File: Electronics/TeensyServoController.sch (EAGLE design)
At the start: 96 parts, among them U1 TEENSY_3.1_ALLPINS, U12 MIC5225, U13 MIC5225, U2 AP3211KTR-G1, U3 AP3211KTR-G1, U4 AP3211KTR-G1, U5 AP2210N-3.3TRG1

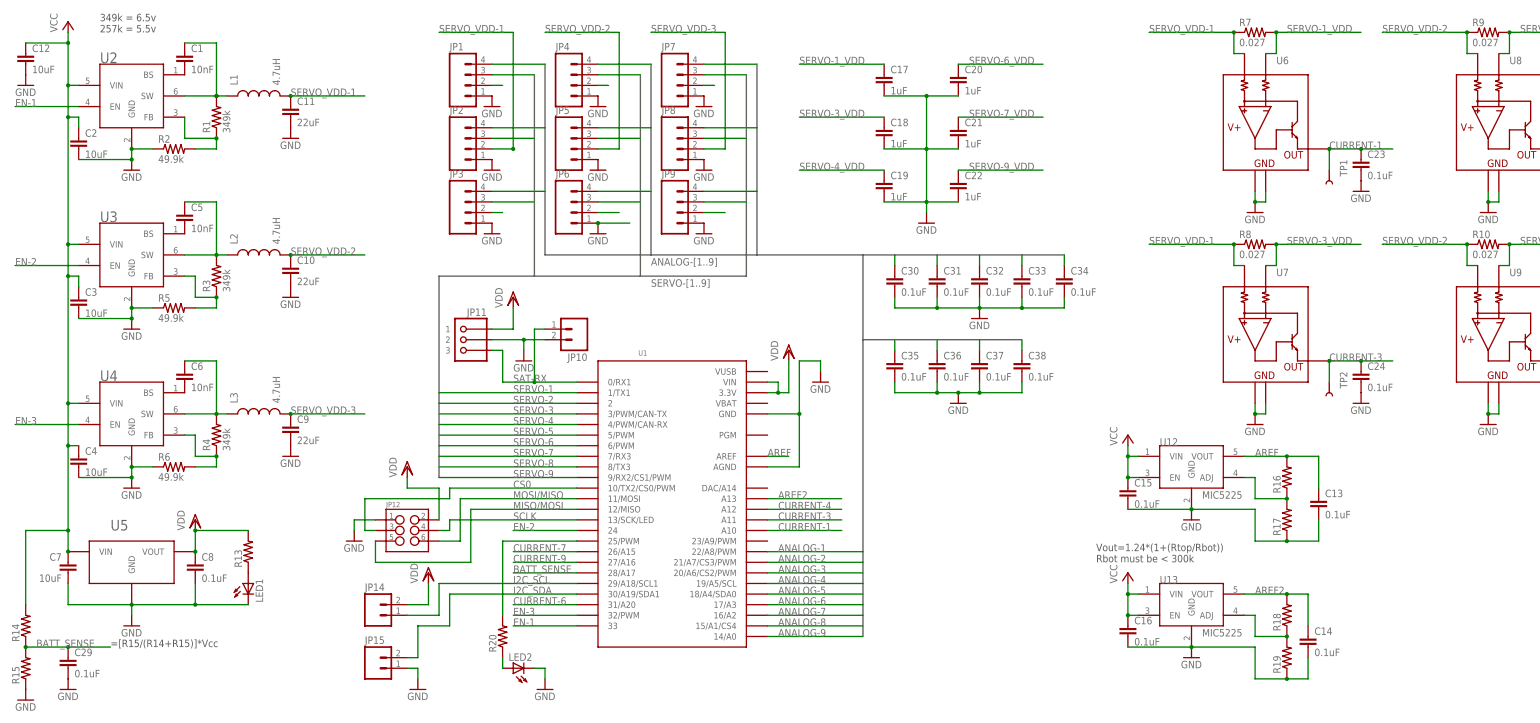
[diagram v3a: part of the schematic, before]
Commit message: Finalized values for most components on PCBs
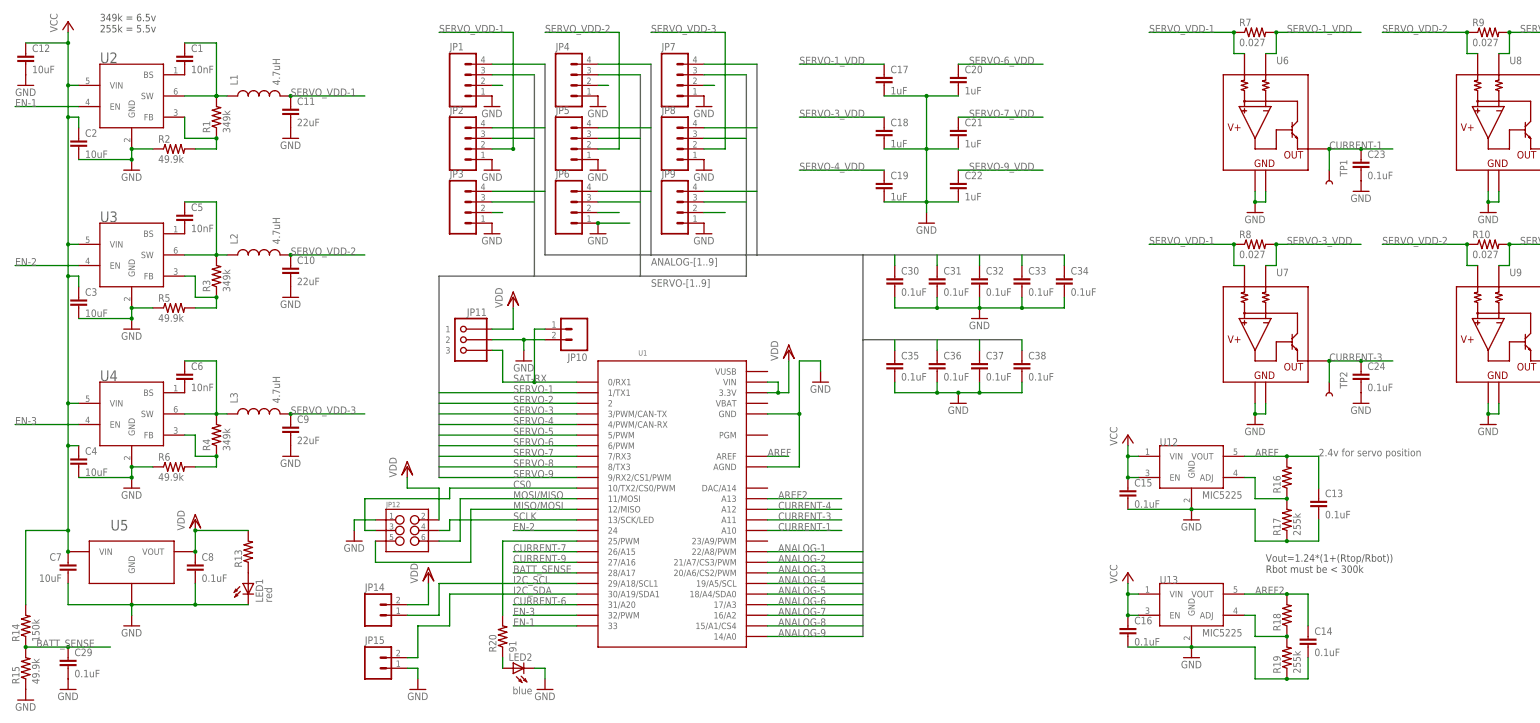
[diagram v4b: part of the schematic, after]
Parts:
- LED1: value (none) -> red
- LED2: value (none) -> blue
- R14: value (none) -> 150k
- R15: value (none) -> 49.9k
- R17, R19: value (none) -> 255k
- R20: value (none) -> 91
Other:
- note added: "2.4v for servo position"
- note added: "349k = 6.5v 255k = 5.5v"
- note removed: "349k = 6.5v 257k = 5.5v"
- note removed: "=[R15/(R14+R15)]*Vcc"
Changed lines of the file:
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@@
 <grid distance="0.1" unitdist="inch" unit="inch" style="lines" multiple="1" display="no" altdistance="0.01" altunitdist="inch" altunit="inch"/>
 <layers>
-<layer number="1" name="Top" color="4" fill="1" visible="yes" active="no"/>
-<layer number="2" name="Route2" color="5" fill="1" visible="yes" active="no"/>
-<layer number="3" name="Route3" color="4" fill="1" visible="yes" active="no"/>
-<layer number="14" name="Route14" color="1" fill="6" visible="yes" active="no"/>
-<layer number="15" name="Route15" color="3" fill="1" visible="yes" active="no"/>
-<layer number="16" name="Bottom" color="1" fill="1" visible="yes" active="no"/>
-<layer number="17" name="Pads" color="2" fill="1" visible="yes" active="no"/>
-<layer number="18" name="Vias" color="2" fill="1" visible="yes" active="no"/>
-<layer number="19" name="Unrouted" color="6" fill="1" visible="yes" active="no"/>
-<layer number="20" name="Dimension" color="15" fill="1" visible="yes" active="no"/>
-<layer number="21" name="tPlace" color="7" fill="1" visible="yes" active="no"/>
-<layer number="22" name="bPlace" color="7" fill="1" visible="yes" active="no"/>
-<layer number="23" name="tOrigins" color="15" fill="1" visible="yes" active="no"/>
-<layer number="24" name="bOrigins" color="15" fill="1" visible="yes" active="no"/>
-<layer number="25" name="tNames" color="7" fill="1" visible="yes" active="no"/>
-<layer number="26" name="bNames" color="7" fill="1" visible="yes" active="no"/>
-<layer number="27" name="tValues" color="7" fill="1" visible="yes" active="no"/>
-<layer number="28" name="bValues" color="7" fill="1" visible="yes" active="no"/>
+<layer number="1" name="Top" color="4" fill="1" visible="no" active="no"/>
+<layer number="2" name="Route2" color="5" fill="1" visible="no" active="no"/>
+<layer number="3" name="Route3" color="4" fill="1" visible="no" active="no"/>
+<layer number="14" name="Route14" color="1" fill="6" visible="no" active="no"/>
+<layer number="15" name="Route15" color="3" fill="1" visible="no" active="no"/>
+<layer number="16" name="Bottom" color="1" fill="1" visible="no" active="no"/>
+<layer number="17" name="Pads" color="2" fill="1" visible="no" active="no"/>
+<layer number="18" name="Vias" color="2" fill="1" visible="no" active="no"/>
+<layer number="19" name="Unrouted" color="6" fill="1" visible="no" active="no"/>
+<layer number="20" name="Dimension" color="15" fill="1" visible="no" active="no"/>
+<layer number="21" name="tPlace" color="7" fill="1" visible="no" active="no"/>
+<layer number="22" name="bPlace" color="7" fill="1" visible="no" active="no"/>
+<layer number="23" name="tOrigins" color="15" fill="1" visible="no" active="no"/>
+<layer number="24" name="bOrigins" color="15" fill="1" visible="no" active="no"/>
+<layer number="25" name="tNames" color="7" fill="1" visible="no" active="no"/>
+<layer number="26" name="bNames" color="7" fill="1" visible="no" active="no"/>
+<layer number="27" name="tValues" color="7" fill="1" visible="no" active="no"/>
+<layer number="28" name="bValues" color="7" fill="1" visible="no" active="no"/>
 <layer number="29" name="tStop" color="7" fill="3" visible="no" active="no"/>
 <layer number="30" name="bStop" color="7" fill="6" visible="no" active="no"/>
@@
 <layer number="35" name="tGlue" color="7" fill="4" visible="no" active="no"/>
 <layer number="36" name="bGlue" color="7" fill="5" visible="no" active="no"/>
-<layer number="37" name="tTest" color="7" fill="1" visible="yes" active="no"/>
-<layer number="38" name="bTest" color="7" fill="1" visible="yes" active="no"/>
+<layer number="37" name="tTest" color="7" fill="1" visible="no" active="no"/>
+<layer number="38" name="bTest" color="7" fill="1" visible="no" active="no"/>
 <layer number="39" name="tKeepout" color="4" fill="11" visible="no" active="no"/>
 <layer number="40" name="bKeepout" color="1" fill="11" visible="no" active="no"/>
@@
 <layer number="44" name="Drills" color="7" fill="1" visible="no" active="no"/>
 <layer number="45" name="Holes" color="7" fill="1" visible="no" active="no"/>
-<layer number="46" name="Milling" color="3" fill="1" visible="yes" active="no"/>
-<layer number="47" name="Measures" color="7" fill="1" visible="yes" active="no"/>
-<layer number="48" name="Document" color="7" fill="1" visible="yes" active="no"/>
-<layer number="49" name="Reference" color="7" fill="1" visible="yes" active="no"/>
-<layer number="50" name="dxf" color="7" fill="1" visible="yes" active="no"/>
-<layer number="51" name="tDocu" color="7" fill="1" visible="yes" active="no"/>
-<layer number="52" name="bDocu" color="7" fill="1" visible="yes" active="no"/>
-<layer number="53" name="tGND_GNDA" color="7" fill="9" visible="yes" active="no"/>
-<layer number="54" name="bGND_GNDA" color="1" fill="9" visible="yes" active="no"/>
-<layer number="56" name="wert" color="7" fill="1" visible="yes" active="no"/>
+<layer number="46" name="Milling" color="3" fill="1" visible="no" active="no"/>
+<layer number="47" name="Measures" color="7" fill="1" visible="no" active="no"/>
+<layer number="48" name="Document" color="7" fill="1" visible="no" active="no"/>
+<layer number="49" name="Reference" color="7" fill="1" visible="no" active="no"/>
+<layer number="50" name="dxf" color="7" fill="1" visible="no" active="no"/>
+<layer number="51" name="tDocu" color="7" fill="1" visible="no" active="no"/>
+<layer number="52" name="bDocu" color="7" fill="1" visible="no" active="no"/>
+<layer number="53" name="tGND_GNDA" color="7" fill="9" visible="no" active="no"/>
+<layer number="54" name="bGND_GNDA" color="1" fill="9" visible="no" active="no"/>
+<layer number="56" name="wert" color="7" fill="1" visible="no" active="no"/>
 <layer number="90" name="Modules" color="5" fill="1" visible="yes" active="yes"/>
 <layer number="91" name="Nets" color="2" fill="1" visible="yes" active="yes"/>
@@
 <part name="GND21" library="supply1" deviceset="GND" device=""/>
 <part name="GND22" library="supply1" deviceset="GND" device=""/>
-<part name="LED1" library="SparkFun-LED" deviceset="LED" device="0603"/>
+<part name="LED1" library="SparkFun-LED" deviceset="LED" device="0603" value="red"/>
 <part name="R13" library="resistor" deviceset="R-US_" device="R0402"/>
-<part name="R15" library="resistor" deviceset="R-US_" device="R0402"/>
+<part name="R15" library="resistor" deviceset="R-US_" device="R0402" value="49.9k"/>
 <part name="GND23" library="supply1" deviceset="GND" device=""/>
-<part name="R14" library="resistor" deviceset="R-US_" device="R0402"/>
+<part name="R14" library="resistor" deviceset="R-US_" device="R0402" value="150k"/>
 <part name="VDD1" library="supply1" deviceset="VDD" device=""/>
 <part name="C9" library="resistor" deviceset="C-EU" device="C0603" value="22uF"/>
@@
 <part name="GND29" library="supply1" deviceset="GND" device=""/>
 <part name="R16" library="resistor" deviceset="R-US_" device="R0603"/>
-<part name="R17" library="resistor" deviceset="R-US_" device="R0603"/>
+<part name="R17" library="resistor" deviceset="R-US_" device="R0603" value="255k"/>
 <part name="U13" library="My Parts" deviceset="MIC5225" device=""/>
 <part name="P+3" library="supply1" deviceset="VCC" device=""/>
 <part name="GND30" library="supply1" deviceset="GND" device=""/>
 <part name="R18" library="resistor" deviceset="R-US_" device="R0603"/>
-<part name="R19" library="resistor" deviceset="R-US_" device="R0603"/>
+<part name="R19" library="resistor" deviceset="R-US_" device="R0603" value="255k"/>
 <part name="JP14" library="SparkFun-Connectors" deviceset="M02" device="PTH"/>
 <part name="JP15" library="SparkFun-Connectors" deviceset="M02" device="PTH"/>
@@
 <part name="C15" library="resistor" deviceset="C-EU" device="C0603" value="0.1uF"/>
 <part name="C16" library="resistor" deviceset="C-EU" device="C0603" value="0.1uF"/>
-<part name="LED2" library="SparkFun-LED" deviceset="LED" device="0603"/>
-<part name="R20" library="resistor" deviceset="R-US_" device="R0402"/>
+<part name="LED2" library="SparkFun-LED" deviceset="LED" device="0603" value="blue"/>
+<part name="R20" library="resistor" deviceset="R-US_" device="R0402" value="91"/>
 <part name="GND31" library="supply1" deviceset="GND" device=""/>
 <part name="C17" library="resistor" deviceset="C-EU" device="C0603" value="1uF"/>
@@
 <plain>
 <text x="22.86" y="114.3" size="1.778" layer="97">349k = 6.5v
-257k = 5.5v</text>
-<text x="25.4" y="-33.02" size="1.778" layer="97">=[R15/(R14+R15)]*Vcc</text>
-<text x="261.62" y="-12.7" size="1.778" layer="97">Vout=1.24*(1+(Rtop/Rbot))
+255k = 5.5v</text>
+<text x="302.26" y="-15.24" size="1.778" layer="97">Vout=1.24*(1+(Rtop/Rbot))
 Rbot must be &lt; 300k</text>
+<text x="314.96" y="12.7" size="1.778" layer="96">2.4v for servo position</text>
 </plain>
 <instances>
@@
 <instance part="C15" gate="G$1" x="269.24" y="5.08"/>
 <instance part="C16" gate="G$1" x="269.24" y="-27.94"/>
-<instance part="LED2" gate="G$1" x="121.92" y="-38.1" rot="R90"/>
+<instance part="LED2" gate="G$1" x="121.92" y="-38.1" smashed="yes" rot="R90">
+<attribute name="NAME" x="126.492" y="-34.544" size="1.778" layer="95" rot="R180"/>
+<attribute name="VALUE" x="126.492" y="-42.545" size="1.778" layer="96" rot="R180"/>
+</instance>
 <instance part="R20" gate="G$1" x="119.38" y="-30.48" rot="R90"/>
 <instance part="GND31" gate="1" x="129.54" y="-43.18"/>
